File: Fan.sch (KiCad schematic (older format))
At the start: 9 parts

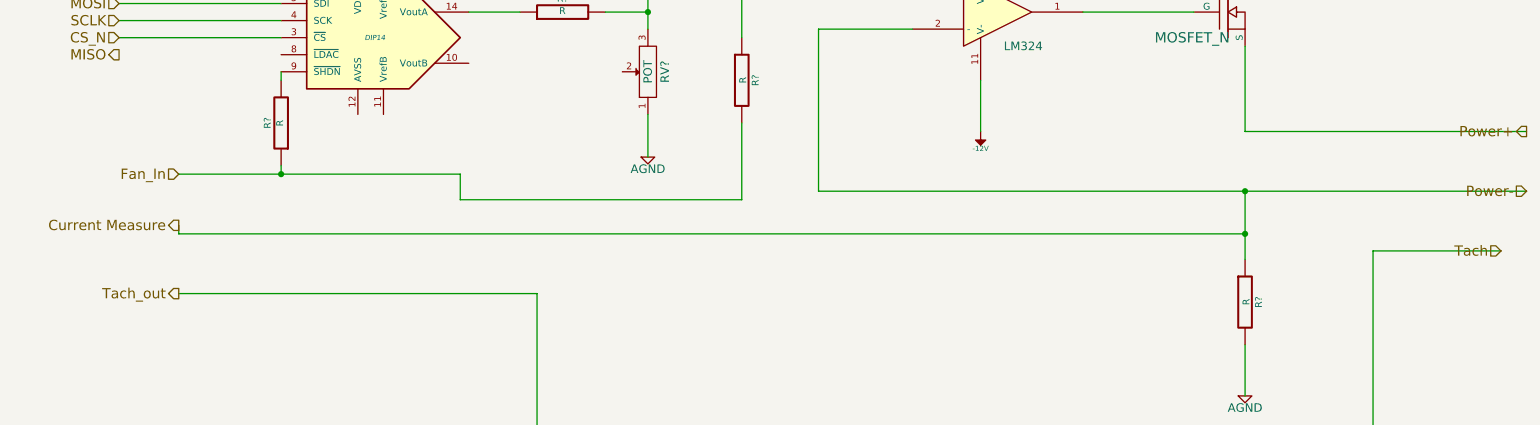
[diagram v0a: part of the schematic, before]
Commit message: Changes up to and including Arduino module
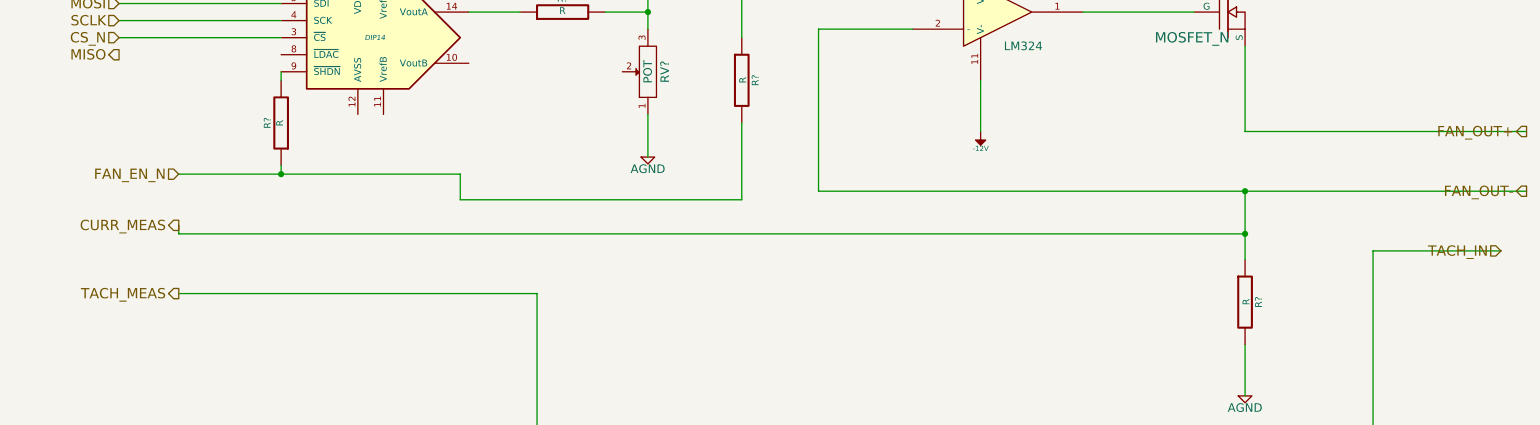
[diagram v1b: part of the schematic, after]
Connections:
- net Current Measure renamed CURR_MEAS
- net Fan_In renamed FAN_EN_N
- net Power+ renamed FAN_OUT+
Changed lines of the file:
@@
 LIBS:valves
 LIBS:BencyBuddy
+LIBS:arduino_shieldsNCL
 LIBS:BenchBuddy-cache
 EELAYER 27 0
@@
 Sheet 6 9
 Title ""
-Date "9 feb 2014"
+Date "12 feb 2014"
 Rev ""
 Comp ""
@@
 $EndDescr
 Text HLabel 9350 3050 0    60   Output ~ 0
-Power+
-Text HLabel 9350 3400 0    60   Input ~ 0
-Power-
+FAN_OUT+
+Text HLabel 9350 3400 0    60   Output ~ 0
+FAN_OUT-
 Text HLabel 9200 3750 0    60   Input ~ 0
-Tach
+TACH_IN
 Text HLabel 1450 4000 0    60   Output ~ 0
-Tach_out
+TACH_MEAS
 Text HLabel 1450 3300 0    60   Input ~ 0
-Fan_In
+FAN_EN_N
 $Comp
 L LM324 U?
@@
 	3550 4000 1450 4000
 Text HLabel 1450 3600 0    60   Output ~ 0
-Current Measure
+CURR_MEAS
 Wire Wire Line
 	1450 3650 7700 3650

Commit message: Current/Fan updates
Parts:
- removed R? (x3): R, ~, symbol R
- removed RV?: POT, ~, symbol POT
- added D?: DIODE, ~, symbol DIODE
- added Q? (x2): MOSFET_N, ~, symbol MOSFET_N
- added TH?: THERMISTOR, ~, symbol THERMISTOR
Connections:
- net +12V: no longer Q?.D
- net AGND: now also Q?.S, Q?.S
- net CURR_MEAS: now also Q?.S, Q?.D
- net FAN_OUT+: now also D?.2 (K), TH?.2; no longer Q?.S
- net at R?.2, U?.3 (+): now also Q?.D
- new net +12C: TH?.1
- new net FAN_MODE: Q?.G
- new net FAN_OUT-: D?.1 (A), Q?.D
- new net FAN_PWM: Q?.G
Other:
- moved on the sheet: R?, U?
